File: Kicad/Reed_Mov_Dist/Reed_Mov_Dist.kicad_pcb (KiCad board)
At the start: 2 copper layers, 22 parts, among them J1 Barrel_Jack, J10 HC-SRO4, J11 URM37, J12 LV-MaxSonar-EZ1, J13 Conn_01x02, J2 Conn_01x02, J3 Conn_01x02, J4 Conn_01x02, J5 LIS3DH_1, J6 ITG3200, J7 LIS3DH_2, J8 TTL_Level_Shifter_1, J9 TTL_Level_Shifter_2, U1 LM7805_TO220, U2 XBEE

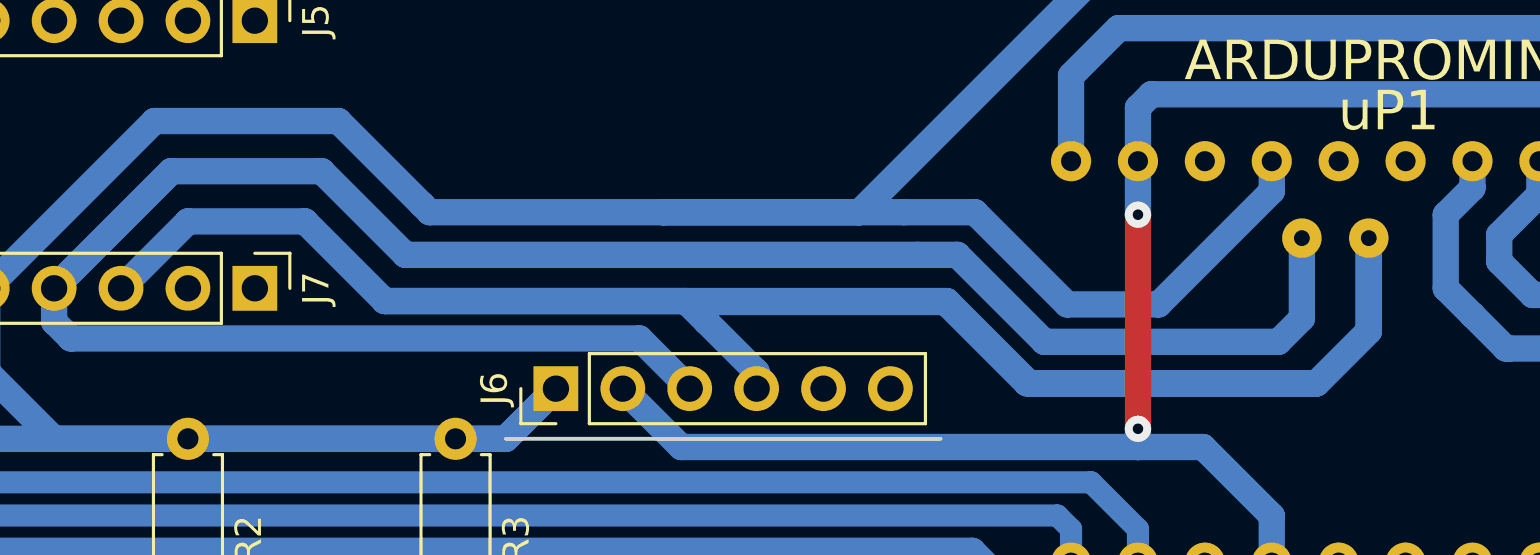
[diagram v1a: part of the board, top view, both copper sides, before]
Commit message: Corrected SDA and SCL switched bug.
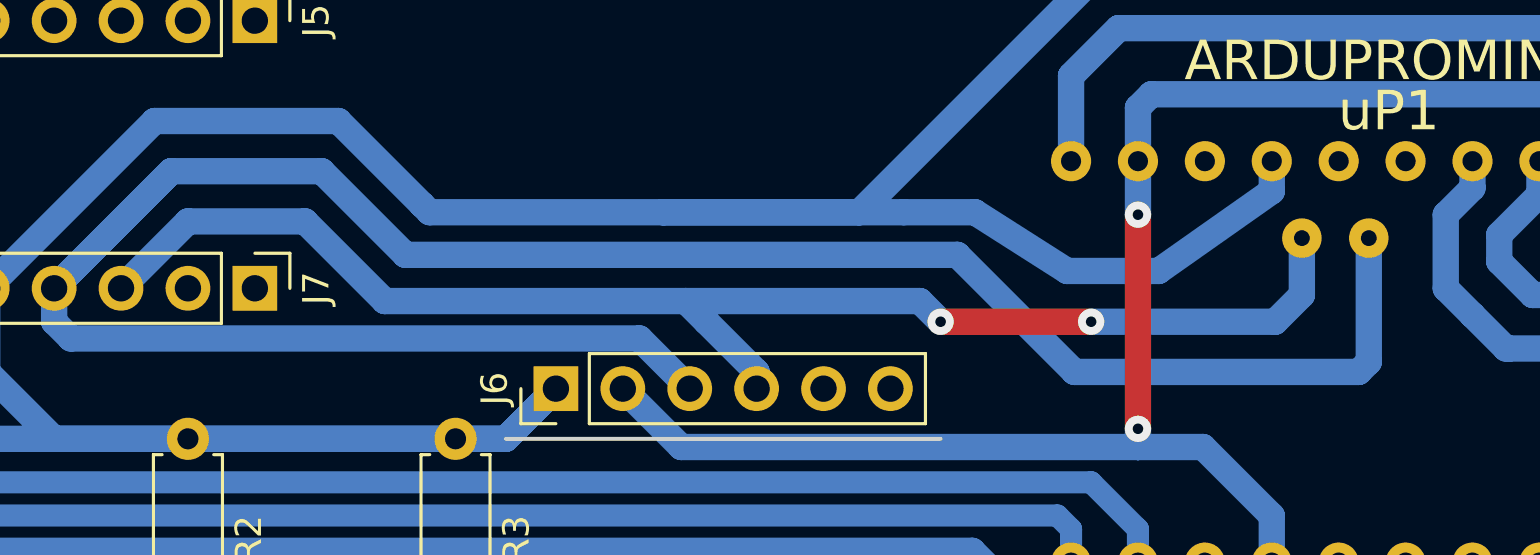
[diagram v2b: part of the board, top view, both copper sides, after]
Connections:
- uP1 pad 31: SDA -> SCL
- uP1 pad 32: SCL -> SDA
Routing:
- net SCL: track 102.8 -> 54.7 mm, vias 0 -> 2
- net SDA: track 88.3 -> 92.5 mm
- net 3V3: track 205.1 -> 203.5 mm
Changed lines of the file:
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@@
     (thickness 1.6)
     (drawings 6)
-    (tracks 236)
+    (tracks 232)
     (zones 0)
     (modules 22)
@@
     (pad 30 thru_hole circle (at 17.78 34.29 90) (size 1.524 1.524) (drill 0.762) (layers *.Cu *.Mask F.SilkS))
     (pad 31 thru_hole circle (at 14.859 15.113 90) (size 1.5 1.5) (drill 0.6) (layers *.Cu *.Mask F.SilkS)
+      (net 10 SCL))
+    (pad 32 thru_hole circle (at 14.859 17.653 90) (size 1.5 1.5) (drill 0.6) (layers *.Cu *.Mask F.SilkS)
       (net 9 SDA))
-    (pad 32 thru_hole circle (at 14.859 17.653 90) (size 1.5 1.5) (drill 0.6) (layers *.Cu *.Mask F.SilkS)
-      (net 10 SCL))
     (pad 34 thru_hole circle (at 14.859 25.527 90) (size 1.5 1.5) (drill 0.6) (layers *.Cu *.Mask F.SilkS))
     (pad 35 thru_hole circle (at 14.859 28.067 90) (size 1.5 1.5) (drill 0.6) (layers *.Cu *.Mask F.SilkS))
@@
   (segment (start 82.931 85.725) (end 85.598 88.392) (width 1) (layer B.Cu) (net 7))
   (segment (start 67.31 85.725) (end 67.31 88.9) (width 1) (layer B.Cu) (net 7))
-  (segment (start 43.815 78.105) (end 46.99 78.105) (width 1) (layer B.Cu) (net 8) (status C00000))
+  (segment (start 43.815 78.105) (end 46.99 78.105) (width 1) (layer B.Cu) (net 8))
   (segment (start 67.31 78.105) (end 69.215 78.105) (width 1) (layer B.Cu) (net 8))
   (segment (start 69.215 78.105) (end 71.12 76.2) (width 1) (layer B.Cu) (net 8))
@@
   (segment (start 132.08 64.77) (end 130.81 66.04) (width 1) (layer B.Cu) (net 8))
   (segment (start 84.328 69.5025) (end 87.0285 69.5025) (width 1) (layer B.Cu) (net 8))
-  (segment (start 94.003002 73.001998) (end 98.298 68.707) (width 1) (layer B.Cu) (net 8))
-  (segment (start 90.527998 73.001998) (end 94.003002 73.001998) (width 1) (layer B.Cu) (net 8))
-  (segment (start 87.0285 69.5025) (end 90.527998 73.001998) (width 1) (layer B.Cu) (net 8))
+  (segment (start 94.003002 71.731998) (end 98.298 68.707) (width 1) (layer B.Cu) (net 8))
+  (segment (start 90.527998 71.731998) (end 94.003002 71.731998) (width 1) (layer B.Cu) (net 8))
+  (segment (start 87.0285 69.5025) (end 90.527998 71.731998) (width 1) (layer B.Cu) (net 8))
   (segment (start 84.328 69.5025) (end 75.184 69.5025) (width 1) (layer B.Cu) (net 8))
   (segment (start 75.184 69.5025) (end 66.3275 69.5025) (width 1) (layer B.Cu) (net 8))
@@
   (segment (start 66.04 69.215) (end 62.865 66.04) (width 1) (layer B.Cu) (net 8))
   (segment (start 62.865 66.04) (end 55.88 66.04) (width 1) (layer B.Cu) (net 8))
-  (segment (start 84.836 71.12) (end 86.36 71.12) (width 1) (layer B.Cu) (net 9))
-  (segment (start 99.441 73.533) (end 99.441 70.485) (width 1) (layer B.Cu) (net 9))
-  (segment (start 98.552 74.422) (end 99.441 73.533) (width 1) (layer B.Cu) (net 9))
-  (segment (start 89.662 74.422) (end 98.552 74.422) (width 1) (layer B.Cu) (net 9))
-  (segment (start 86.36 71.12) (end 89.662 74.422) (width 1) (layer B.Cu) (net 9))
-  (segment (start 65.405 71.12) (end 84.836 71.12) (width 1) (layer B.Cu) (net 9))
-  (segment (start 99.441 70.485) (end 99.441 70.739) (width 1) (layer B.Cu) (net 9))
-  (segment (start 62.23 67.945) (end 56.515 67.945) (width 1) (layer B.Cu) (net 9))
-  (segment (start 65.405 71.12) (end 62.23 67.945) (width 1) (layer B.Cu) (net 9))
+  (segment (start 56.515 67.945) (end 62.23 67.945) (width 1) (layer B.Cu) (net 9))
+  (segment (start 101.981 75.184) (end 101.981 70.485) (width 1) (layer B.Cu) (net 9) (status 800000))
+  (segment (start 101.6 75.565) (end 101.981 75.184) (width 1) (layer B.Cu) (net 9))
+  (segment (start 90.805 75.565) (end 101.6 75.565) (width 1) (layer B.Cu) (net 9))
+  (segment (start 86.36 71.12) (end 90.805 75.565) (width 1) (layer B.Cu) (net 9))
+  (segment (start 65.405 71.12) (end 86.36 71.12) (width 1) (layer B.Cu) (net 9))
+  (segment (start 62.23 67.945) (end 65.405 71.12) (width 1) (layer B.Cu) (net 9))
+  (segment (start 52.07 72.39) (end 52.07 73.66) (width 1) (layer B.Cu) (net 9))
+  (segment (start 52.07 73.66) (end 52.705 74.295) (width 1) (layer B.Cu) (net 9))
+  (segment (start 52.705 74.295) (end 74.295 74.295) (width 1) (layer B.Cu) (net 9))
+  (segment (start 74.295 74.295) (end 76.2 76.2) (width 1) (layer B.Cu) (net 9))
   (segment (start 56.515 67.945) (end 52.07 72.39) (width 1) (layer B.Cu) (net 9))
-  (segment (start 52.07 72.39) (end 52.07 73.66) (width 1) (layer B.Cu) (net 9))
-  (segment (start 74.295 74.295) (end 76.2 76.2) (width 1) (layer B.Cu) (net 9))
-  (segment (start 52.705 74.295) (end 74.295 74.295) (width 1) (layer B.Cu) (net 9))
-  (segment (start 52.07 73.66) (end 52.705 74.295) (width 1) (layer B.Cu) (net 9))
   (segment (start 56.515 67.945) (end 52.07 72.39) (width 1) (layer B.Cu) (net 9))
-  (segment (start 64.619998 72.874998) (end 85.962498 72.874998) (width 1) (layer B.Cu) (net 10))
-  (segment (start 89.0875 76) (end 100 76) (width 1) (layer B.Cu) (net 10))
-  (segment (start 85.962498 72.874998) (end 89.0875 76) (width 1) (layer B.Cu) (net 10))
-  (segment (start 100 76) (end 101.981 74.019) (width 1) (layer B.Cu) (net 10))
-  (segment (start 101.981 74.019) (end 101.981 70.485) (width 1) (layer B.Cu) (net 10))
-  (segment (start 86 72.9125) (end 86 73) (width 1) (layer B.Cu) (net 10))
-  (segment (start 76.0875 72.9125) (end 86 72.9125) (width 1) (layer B.Cu) (net 10))
-  (segment (start 86 73) (end 89 76) (width 1) (layer B.Cu) (net 10))
-  (segment (start 89 76) (end 100 76) (width 1) (layer B.Cu) (net 10))
-  (segment (start 101.981 74.019) (end 101.981 70.485) (width 1) (layer B.Cu) (net 10))
-  (segment (start 100 76) (end 101.981 74.019) (width 1) (layer B.Cu) (net 10))
-  (segment (start 78.74 76.2) (end 78.74 75.565) (width 1) (layer B.Cu) (net 10))
+  (segment (start 99.441 70.485) (end 99.441 72.644) (width 1) (layer B.Cu) (net 10) (status 400000))
+  (segment (start 84.939998 72.874998) (end 76.049998 72.874998) (width 1) (layer B.Cu) (net 10))
+  (segment (start 85.725 73.66) (end 84.939998 72.874998) (width 1) (layer B.Cu) (net 10))
+  (via (at 85.725 73.66) (size 1) (drill 0.4) (layers F.Cu B.Cu) (net 10))
+  (segment (start 91.44 73.66) (end 85.725 73.66) (width 1) (layer F.Cu) (net 10))
+  (via (at 91.44 73.66) (size 1) (drill 0.4) (layers F.Cu B.Cu) (net 10))
+  (segment (start 98.425 73.66) (end 91.44 73.66) (width 1) (layer B.Cu) (net 10))
+  (segment (start 99.441 72.644) (end 98.425 73.66) (width 1) (layer B.Cu) (net 10))
+  (segment (start 64.619998 72.874998) (end 61.595 69.85) (width 1) (layer B.Cu) (net 10))
+  (segment (start 57.15 69.85) (end 54.61 72.39) (width 1) (layer B.Cu) (net 10))
+  (segment (start 76.049998 72.874998) (end 64.619998 72.874998) (width 1) (layer B.Cu) (net 10))
+  (segment (start 61.595 69.85) (end 57.15 69.85) (width 1) (layer B.Cu) (net 10))
+  (segment (start 76.0875 72.9125) (end 76.049998 72.874998) (width 1) (layer B.Cu) (net 10))
   (segment (start 78.74 75.565) (end 76.835 73.66) (width 1) (layer B.Cu) (net 10))
   (segment (start 76.835 73.66) (end 76.0875 72.9125) (width 1) (layer B.Cu) (net 10))
-  (segment (start 76.0875 72.9125) (end 76.049998 72.874998) (width 1) (layer B.Cu) (net 10))
-  (segment (start 64.619998 72.874998) (end 61.595 69.85) (width 1) (layer B.Cu) (net 10))
-  (segment (start 76.049998 72.874998) (end 64.619998 72.874998) (width 1) (layer B.Cu) (net 10))
-  (segment (start 57.15 69.85) (end 54.61 72.39) (width 1) (layer B.Cu) (net 10))
-  (segment (start 61.595 69.85) (end 57.15 69.85) (width 1) (layer B.Cu) (net 10))
+  (segment (start 99.441 70.485) (end 99.441 70.739) (width 1) (layer B.Cu) (net 10))
+  (segment (start 78.74 76.2) (end 78.74 75.565) (width 1) (layer B.Cu) (net 10))
   (segment (start 149.86 71.12) (end 143.002 71.12) (width 1) (layer B.Cu) (net 11))
   (segment (start 119.126 74.676) (end 110.998 82.804) (width 1) (layer B.Cu) (net 11))
@@
   (segment (start 90.160002 81.016002) (end 90.678 81.534) (width 0.84) (layer B.Cu) (net 23))
   (segment (start 31.75 81.016002) (end 90.160002 81.016002) (width 0.84) (layer B.Cu) (net 23))
-  (segment (start 41.275 78.105) (end 26.035 78.105) (width 1) (layer B.Cu) (net 24) (status 400000))
-  (segment (start 20.955 83.185) (end 20.955 86.36) (width 1) (layer B.Cu) (net 24) (status 800000))
+  (segment (start 41.275 78.105) (end 26.035 78.105) (width 1) (layer B.Cu) (net 24))
+  (segment (start 20.955 83.185) (end 20.955 86.36) (width 1) (layer B.Cu) (net 24))
   (segment (start 26.035 78.105) (end 20.955 83.185) (width 1) (layer B.Cu) (net 24))
   (zone (net 2) (net_name GND) (layer B.Cu) (hatch edge 0.508)
